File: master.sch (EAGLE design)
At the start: 314 parts, among them IC1001 AQV252G2S, IC1002 AQV252G2S, IC1003 AQV252G2S, IC1004 AQV252G2S, IC1005 AQV252G2S, IC1006 AQV252G2S, IC1101 UA78L05ACPK, IC1102 ADUM3300ARW, IC1103 ADUM3300ARW, IC1401 IP4220CZ6, IC1402 FT231XS-R, IC1403 ADUM3401ARW, IC1404 IP4220CZ6, IC1405 FT231XS-R, IC1406 ADUM3401ARW, IC1501 AT25128B-SSHL-T, IC1801 IS42S16400J-5TL, IC201 LM1085IS-5.0/NOPB, IC202 MURATA_NCS6S1205C, IC301 LM1085IS-5.0/NOPB, IC302 RS-2405D/H2, IC401 ADR3425ARJZ, IC402 STM32F429IIT6, IC501 STM32F429VIT6, IC601 ADUM3401ARW, IC701 UA78L05ACPK, IC702 ADUM3301ARW, IC801 KA7805ERTF, IC802 TJA1052IT/1Y, IC803 CPC1008N, IC901 LM317MBSTT3G, IC902 CPC1008N, IC903 CPC1008N, IC904 CPC1008N, IC905 CPC1008N, Q401 7B-8.000MAAJ-T, Q501 7B-8.000MAAJ-T, T1001 IRLML0100TRPBF, T1002 IRLML0100TRPBF, T1003 IRLML0100TRPBF, T1004 IRLML0100TRPBF, T1005 IRLML0100TRPBF, T1006 IRLML0100TRPBF, T201 TISP40XXH1BJ, T401 BSS84P, T501 BSS84P, T701 IRLML0100TRPBF, T801 IRLML0100TRPBF, T901 BUK964R8-60E, T902 IRLML0100TRPBF, T903 IRLML0100TRPBF, X1201 43045-0400_MOLEX_4PIN, X1202 43045-0400_MOLEX_4PIN, X1203 43045-0400_MOLEX_4PIN, X1204 43045-0400_MOLEX_4PIN, X1205 43045-0400_MOLEX_4PIN, X1206 43045-0400_MOLEX_4PIN, X1401 MINI-USB-2.0, X1402 MINI-USB-2.0, X1601 43045-1600_MOLEX_16PIN, X201 43045-0600_MOLEX_6PIN, X402 MA02-1, X403 SAMTEC_FTS_20POL_HEADER_VERTI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, X501 MA02-1, X502 SAMTEC_FTS_20POL_HEADER_VERTI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, X701 43045-0400_MOLEX_4PIN, X801 43045-0400_MOLEX_4PIN, X901 43045-0200_MOLEX_2PIN, X902 MA02-1SMALL_PINS_OUTLINE

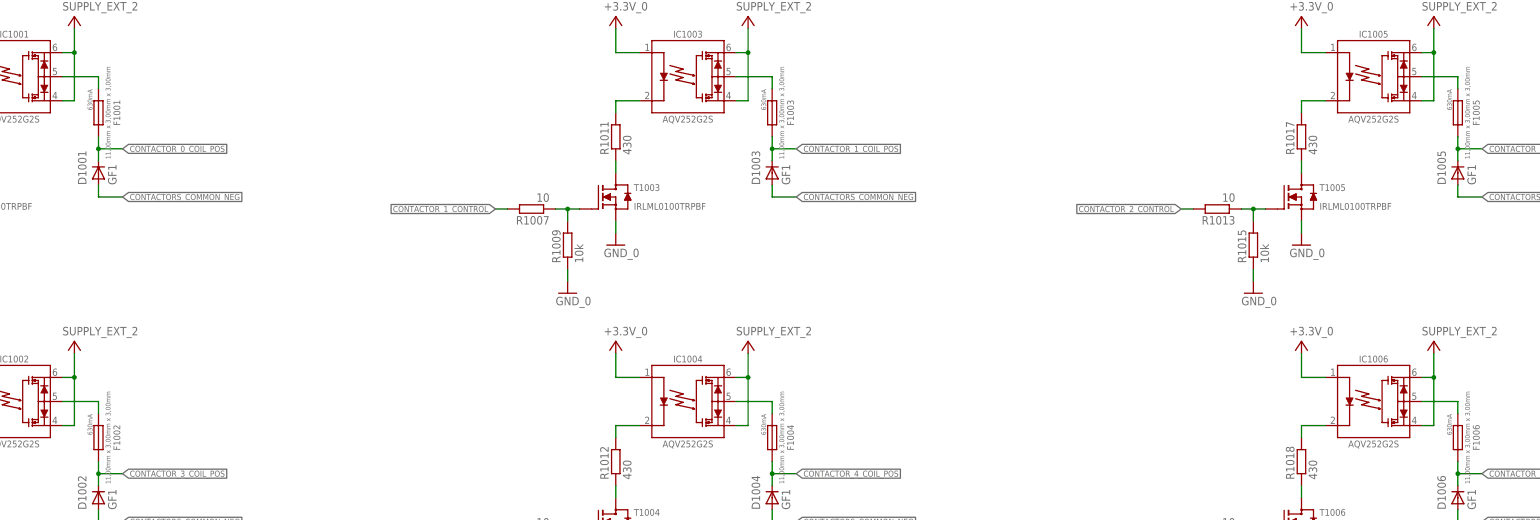
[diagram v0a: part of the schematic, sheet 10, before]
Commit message: fixed fuse value in schematic
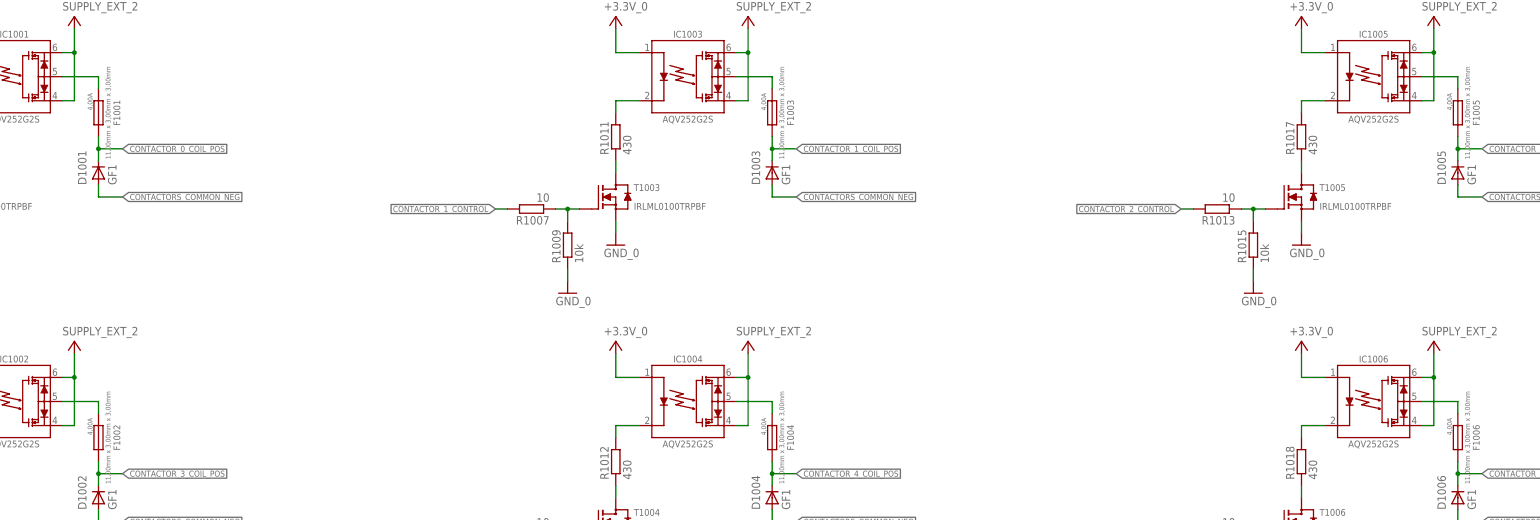
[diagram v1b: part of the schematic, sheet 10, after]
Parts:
- F1001, F1002, F1003, F1004, F1005, F1006: value 630MA_UMT -> 4,00A_UMT; device foxBMS_BMS-Master:630MA_UMT -> foxBMS_BMS-Master:4,00A_UMT
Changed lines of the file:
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@@
 <setting verticaltext="up"/>
 </settings>
-<grid distance="0.1" unitdist="inch" unit="inch" style="lines" multiple="1" display="no" altdistance="0.01" altunitdist="inch" altunit="inch"/>
+<grid distance="100" unitdist="mil" unit="mil" style="lines" multiple="1" display="yes" altdistance="10" altunitdist="mil" altunit="mil"/>
 <layers>
-<layer number="1" name="Top" color="4" fill="1" visible="no" active="no"/>
-<layer number="2" name="Route2" color="1" fill="3" visible="no" active="no"/>
-<layer number="3" name="Route3" color="4" fill="3" visible="no" active="no"/>
-<layer number="4" name="Route4" color="1" fill="4" visible="no" active="no"/>
-<layer number="5" name="Route5" color="4" fill="4" visible="no" active="no"/>
-<layer number="6" name="Route6" color="1" fill="8" visible="no" active="no"/>
-<layer number="7" name="Route7" color="4" fill="8" visible="no" active="no"/>
-<layer number="8" name="Route8" color="1" fill="2" visible="no" active="no"/>
-<layer number="9" name="Route9" color="4" fill="2" visible="no" active="no"/>
-<layer number="10" name="Route10" color="1" fill="7" visible="no" active="no"/>
-<layer number="11" name="Route11" color="4" fill="7" visible="no" active="no"/>
-<layer number="12" name="Route12" color="1" fill="5" visible="no" active="no"/>
-<layer number="13" name="Route13" color="4" fill="5" visible="no" active="no"/>
-<layer number="14" name="Route14" color="1" fill="6" visible="no" active="no"/>
-<layer number="15" name="Route15" color="4" fill="6" visible="no" active="no"/>
-<layer number="16" name="Bottom" color="1" fill="1" visible="no" active="no"/>
-<layer number="17" name="Pads" color="2" fill="1" visible="no" active="no"/>
-<layer number="18" name="Vias" color="2" fill="1" visible="no" active="no"/>
-<layer number="19" name="Unrouted" color="6" fill="1" visible="no" active="no"/>
-<layer number="20" name="Dimension" color="15" fill="1" visible="no" active="no"/>
-<layer number="21" name="tPlace" color="7" fill="1" visible="no" active="no"/>
-<layer number="22" name="bPlace" color="7" fill="1" visible="no" active="no"/>
-<layer number="23" name="tOrigins" color="15" fill="1" visible="no" active="no"/>
-<layer number="24" name="bOrigins" color="15" fill="1" visible="no" active="no"/>
-<layer number="25" name="tNames" color="7" fill="1" visible="no" active="no"/>
-<layer number="26" name="bNames" color="7" fill="1" visible="no" active="no"/>
-<layer number="27" name="tValues" color="7" fill="1" visible="no" active="no"/>
-<layer number="28" name="bValues" color="7" fill="1" visible="no" active="no"/>
+<layer number="1" name="Top" color="4" fill="1" visible="yes" active="no"/>
+<layer number="2" name="Route2" color="1" fill="3" visible="yes" active="no"/>
+<layer number="3" name="Route3" color="4" fill="3" visible="yes" active="no"/>
+<layer number="4" name="Route4" color="1" fill="4" visible="yes" active="no"/>
+<layer number="5" name="Route5" color="4" fill="4" visible="yes" active="no"/>
+<layer number="6" name="Route6" color="1" fill="8" visible="yes" active="no"/>
+<layer number="7" name="Route7" color="4" fill="8" visible="yes" active="no"/>
+<layer number="8" name="Route8" color="1" fill="2" visible="yes" active="no"/>
+<layer number="9" name="Route9" color="4" fill="2" visible="yes" active="no"/>
+<layer number="10" name="Route10" color="1" fill="7" visible="yes" active="no"/>
+<layer number="11" name="Route11" color="4" fill="7" visible="yes" active="no"/>
+<layer number="12" name="Route12" color="1" fill="5" visible="yes" active="no"/>
+<layer number="13" name="Route13" color="4" fill="5" visible="yes" active="no"/>
+<layer number="14" name="Route14" color="1" fill="6" visible="yes" active="no"/>
+<layer number="15" name="Route15" color="4" fill="6" visible="yes" active="no"/>
+<layer number="16" name="Bottom" color="1" fill="1" visible="yes" active="no"/>
+<layer number="17" name="Pads" color="2" fill="1" visible="yes" active="no"/>
+<layer number="18" name="Vias" color="2" fill="1" visible="yes" active="no"/>
+<layer number="19" name="Unrouted" color="6" fill="1" visible="yes" active="no"/>
+<layer number="20" name="Dimension" color="15" fill="1" visible="yes" active="no"/>
+<layer number="21" name="tPlace" color="7" fill="1" visible="yes" active="no"/>
+<layer number="22" name="bPlace" color="7" fill="1" visible="yes" active="no"/>
+<layer number="23" name="tOrigins" color="15" fill="1" visible="yes" active="no"/>
+<layer number="24" name="bOrigins" color="15" fill="1" visible="yes" active="no"/>
+<layer number="25" name="tNames" color="7" fill="1" visible="yes" active="no"/>
+<layer number="26" name="bNames" color="7" fill="1" visible="yes" active="no"/>
+<layer number="27" name="tValues" color="7" fill="1" visible="yes" active="no"/>
+<layer number="28" name="bValues" color="7" fill="1" visible="yes" active="no"/>
 <layer number="29" name="tStop" color="7" fill="3" visible="no" active="no"/>
 <layer number="30" name="bStop" color="7" fill="6" visible="no" active="no"/>
@@
 <layer number="35" name="tGlue" color="7" fill="4" visible="no" active="no"/>
 <layer number="36" name="bGlue" color="7" fill="5" visible="no" active="no"/>
-<layer number="37" name="tTest" color="7" fill="1" visible="no" active="no"/>
-<layer number="38" name="bTest" color="7" fill="1" visible="no" active="no"/>
+<layer number="37" name="tTest" color="7" fill="1" visible="yes" active="no"/>
+<layer number="38" name="bTest" color="7" fill="1" visible="yes" active="no"/>
 <layer number="39" name="tKeepout" color="4" fill="11" visible="no" active="no"/>
 <layer number="40" name="bKeepout" color="1" fill="11" visible="no" active="no"/>
@@
 <layer number="44" name="Drills" color="7" fill="1" visible="no" active="no"/>
 <layer number="45" name="Holes" color="7" fill="1" visible="no" active="no"/>
-<layer number="46" name="Milling" color="3" fill="1" visible="no" active="no"/>
-<layer number="47" name="Measures" color="7" fill="1" visible="no" active="no"/>
-<layer number="48" name="Document" color="7" fill="1" visible="no" active="no"/>
-<layer number="49" name="Reference" color="7" fill="1" visible="no" active="no"/>
-<layer number="50" name="dxf" color="7" fill="1" visible="no" active="no"/>
-<layer number="51" name="tDocu" color="7" fill="1" visible="no" active="no"/>
-<layer number="52" name="bDocu" color="7" fill="1" visible="no" active="no"/>
-<layer number="53" name="tGND_GNDA" color="7" fill="1" visible="no" active="no"/>
-<layer number="54" name="bGND_GNDA" color="7" fill="1" visible="no" active="no"/>
-<layer number="56" name="wert" color="7" fill="1" visible="no" active="no"/>
-<layer number="57" name="tCAD" color="5" fill="1" visible="no" active="no"/>
-<layer number="58" name="bCAD" color="7" fill="1" visible="no" active="no"/>
+<layer number="46" name="Milling" color="3" fill="1" visible="yes" active="no"/>
+<layer number="47" name="Measures" color="7" fill="1" visible="yes" active="no"/>
+<layer number="48" name="Document" color="7" fill="1" visible="yes" active="no"/>
+<layer number="49" name="Reference" color="7" fill="1" visible="yes" active="no"/>
+<layer number="50" name="dxf" color="7" fill="1" visible="yes" active="no"/>
+<layer number="51" name="tDocu" color="7" fill="1" visible="yes" active="no"/>
+<layer number="52" name="bDocu" color="7" fill="1" visible="yes" active="no"/>
+<layer number="53" name="tGND_GNDA" color="7" fill="1" visible="yes" active="no"/>
+<layer number="54" name="bGND_GNDA" color="7" fill="1" visible="yes" active="no"/>
+<layer number="56" name="wert" color="7" fill="1" visible="yes" active="no"/>
+<layer number="57" name="tCAD" color="5" fill="1" visible="yes" active="no"/>
+<layer number="58" name="bCAD" color="7" fill="1" visible="yes" active="no"/>
 <layer number="91" name="Nets" color="2" fill="1" visible="yes" active="yes"/>
 <layer number="92" name="Busses" color="1" fill="1" visible="no" active="yes"/>
@@
 <part name="SUPPLY_EXT_9" library="foxBMS_BMS-Master" deviceset="SUPPLY_EXT_2" device=""/>
 <part name="IC1402" library="foxBMS_BMS-Master" deviceset="FT231X?-*" device="S" technology="R"/>
-<part name="F1001" library="foxBMS_BMS-Master" deviceset="*_UMT" device="" technology="630MA"/>
-<part name="F1003" library="foxBMS_BMS-Master" deviceset="*_UMT" device="" technology="630MA"/>
-<part name="F1005" library="foxBMS_BMS-Master" deviceset="*_UMT" device="" technology="630MA"/>
-<part name="F1006" library="foxBMS_BMS-Master" deviceset="*_UMT" device="" technology="630MA"/>
-<part name="F1004" library="foxBMS_BMS-Master" deviceset="*_UMT" device="" technology="630MA"/>
-<part name="F1002" library="foxBMS_BMS-Master" deviceset="*_UMT" device="" technology="630MA"/>
+<part name="F1001" library="foxBMS_BMS-Master" deviceset="*_UMT" device="" technology="4,00A" value="4,00A_UMT"/>
+<part name="F1003" library="foxBMS_BMS-Master" deviceset="*_UMT" device="" technology="4,00A" value="4,00A_UMT"/>
+<part name="F1005" library="foxBMS_BMS-Master" deviceset="*_UMT" device="" technology="4,00A" value="4,00A_UMT"/>
+<part name="F1006" library="foxBMS_BMS-Master" deviceset="*_UMT" device="" technology="4,00A" value="4,00A_UMT"/>
+<part name="F1004" library="foxBMS_BMS-Master" deviceset="*_UMT" device="" technology="4,00A" value="4,00A_UMT"/>
+<part name="F1002" library="foxBMS_BMS-Master" deviceset="*_UMT" device="" technology="4,00A" value="4,00A_UMT"/>
 <part name="C901" library="foxBMS_BMS-Master" deviceset="C-EU" device="C0805" value="2.2µ"/>
 <part name="R901" library="foxBMS_BMS-Master" deviceset="R-EU_" device="R0603" value="10"/>
